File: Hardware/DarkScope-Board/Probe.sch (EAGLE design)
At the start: 3 parts, among them IC1 TL084D, X1 1-227161-0, X4 2540-5

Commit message: Sim Model DP
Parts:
- IC1: SPICEPREFIX (none) -> X
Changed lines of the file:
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@@
 <part name="P+6" library="supply1" library_urn="urn:adsk.eagle:library:371" deviceset="+5V" device=""/>
 <part name="P-2" library="supply1" library_urn="urn:adsk.eagle:library:371" deviceset="-5V" device=""/>
-<part name="IC1" library="linear" library_urn="urn:adsk.eagle:library:262" deviceset="TL084" device="D" package3d_urn="urn:adsk.eagle:package:16406/2"/>
+<part name="IC1" library="linear" library_urn="urn:adsk.eagle:library:262" deviceset="TL084" device="D" package3d_urn="urn:adsk.eagle:package:16406/2">
+<attribute name="SPICEPREFIX" value="X"/>
+</part>
 <part name="X1" library="con-coax" library_urn="urn:adsk.eagle:library:133" deviceset="?227161*" device="1-" package3d_urn="urn:adsk.eagle:package:6212/1" technology="-0"/>
 </parts>

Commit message: DP Probe SCH
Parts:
- added C1, C2, C6, C7: 0.1u, rcl:C-EUC1206
- added C3: (no value), capacitor-wima:C2,5-3
- added C4, C5: (no value), rcl:C-TRIMM808
- added R1, R12, R4, R9: 10K, rcl:R-US_R0805
- added R10, R13, R2: 3.3K, rcl:R-US_R0805
- added R11, R14, R3: 1.5K, rcl:R-US_R0805
- added R5, R6, R7, R8: (no value), rcl:R-EU_0204/7
- added S1, S2, S3: EG2301, SamacSys_Parts:EG2301
- added TP1, TP2, TP3, TP4: TPB1,27, testpad:TPB1,27
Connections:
- new net N$1: C6.2, S1.1, TP1.TP, X1.1
- new net N$10: S3.3
- new net N$11: R10.1, R9.2, S2.7
- new net N$12: R11.1, S2.6
- new net N$13: R12.2, R13.1, S3.7
- new net N$14: R14.1, S3.6
- new net N$15: IC1B.-IN, IC1B.OUT
- new net N$2: C6.1, S1.3
- new net N$3: R3.1, S1.6
- new net N$4: R1.2, R2.1, S1.7
- new net N$5: C1.2, C2.2, C7.2, R4.1, R5.1, R7.2, S1.2
- new net N$6: C3.1, C4.E, C7.1, R7.1, R8.1, S2.4
- new net N$7: C1.1, R4.2, S2.1
- new net N$8: C2.1, C5.E, R5.2, R6.2, S2.3
- new net N$9: IC1B.+IN, S2.2
- new net VSENSEL1: R11.2, R14.2, TP3.TP, TP4.TP
- net +5V: now also R1.1, R12.1, R9.1, S1.5, S2.5, S3.5
- net CPLSEL: now also R3.2, TP2.TP
- net GND: now also C3.2, C4.A, C5.A, R10.2, R13.2, R2.2, R6.1, R8.2, S1.4, S1.8, S1.MH1, S1.MH2, S1.MH3, S1.MH4, S2.8, S2.MH1, S2.MH2, S2.MH3, S2.MH4, S3.8, S3.MH1, S3.MH2, S3.MH3, S3.MH4, X1.2
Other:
- note added: "AC"
- note added: "DC"
- note added: "GND"
- moved on the sheet: IC1A, IC1B, IC1C, IC1D

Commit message: Drafted Sch for Probe Board
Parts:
- added C8: 120pF, capacitor-wima:C2,5-3
- added C9: 0.1u, capacitor-wima:C2,5-3
- added R15: 300E, rcl:R-EU_0204/7
- added R16: 120e, rcl:R-US_R0805
- added R17: 180E, rcl:R-EU_0204/7
- added R18: 120E, rcl:R-EU_0204/7
- added R19: 1K, rcl:R-US_R0805
- added R20: 3K, rcl:R-US_R0805
- added R21: 150E, rcl:R-US_R0805
- added R22: 120E, rcl:R-US_R0805
- added R23: 100k, rcl:R-US_R0805
- added R24: 100K, rcl:R-US_R0805
- added R25: 1k, rcl:R-US_R0805
- added TP5, TP6, TP7, TP8: TPB1,27, testpad:TPB1,27
- C1: value 0.1u -> 220pF
- C2: value 0.1u -> 3pF
- C3: value (none) -> 120pF
- C4, C5: value (none) -> 30pF
- C7: value 0.1u -> 1pF
- R4: value 10K -> 100K
- R5: value (none) -> 1.8M 1%
- R6: value (none) -> 200K 1%
- R7: value (none) -> 2M 1%
- R8: value (none) -> 20K 1%
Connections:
- removed net VSENSEL3: X4-24.KL
- removed net VSENSEL4: X4-25.KL
- new net N$16: IC1C.+IN, S3.2
- new net N$17: R17.1, R18.2, S3.4
- new net N$19: S3.1
- new net N$20: IC1C.-IN, R19.1, R20.1, R21.1
- new net N$22: IC1D.+IN, R16.2, R23.1
- new net N$23: IC1C.OUT, R16.1, R19.2, R22.1
- new net N$24: C9.1, IC1D.-IN, R24.1, TP7.TP
- new net N&123: IC1D.OUT, R23.2, R25.1, TP6.TP
- new net VSENSEL2: R14.2, TP4.TP, X4-25.KL
- net -5V: now also R20.2
- net ADCIN: now also C8.1, R22.2
- net GND: now also C8.2, C9.2, R18.1, R21.2
- net N$10: now also R15.1, R17.2
- net N$15: now also R15.2, TP5.TP
- net TL_PWM: now also R24.2
- net TRIG: now also R25.2
- net VSENSEL1: now also X4-24.KL; no longer R14.2, TP4.TP
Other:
- moved on the sheet: IC1C, IC1D, R12, R13, R14, S3, TP4

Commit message: DP wtf
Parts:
- added C10, C11: 0.1uF, rcl:C-EUC1206
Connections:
- net +5V: now also C10.2, IC1P.V+
- net -5V: now also C11.2, IC1P.V-
- net GND: now also C10.1, C11.1
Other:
- note added: "0.1V"
- note added: "10mV"
- note added: "1V"
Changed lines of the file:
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@@
 <part name="TP7" library="testpad" library_urn="urn:adsk.eagle:library:385" deviceset="TP" device="B1,27" package3d_urn="urn:adsk.eagle:package:27944/2"/>
 <part name="TP8" library="testpad" library_urn="urn:adsk.eagle:library:385" deviceset="TP" device="B1,27" package3d_urn="urn:adsk.eagle:package:27944/2"/>
+<part name="C10" library="rcl" library_urn="urn:adsk.eagle:library:334" deviceset="C-EU" device="C1206" package3d_urn="urn:adsk.eagle:package:23618/2" value="0.1uF"/>
+<part name="C11" library="rcl" library_urn="urn:adsk.eagle:library:334" deviceset="C-EU" device="C1206" package3d_urn="urn:adsk.eagle:package:23618/2" value="0.1uF"/>
+<part name="P+1" library="supply1" library_urn="urn:adsk.eagle:library:371" deviceset="+5V" device=""/>
+<part name="P-3" library="supply1" library_urn="urn:adsk.eagle:library:371" deviceset="-5V" device=""/>
+<part name="P-4" library="supply1" library_urn="urn:adsk.eagle:library:371" deviceset="-5V" device=""/>
+<part name="GND12" library="supply1" library_urn="urn:adsk.eagle:library:371" deviceset="GND" device=""/>
 </parts>
 <sheets>
@@
 <instance part="P-2" gate="1" x="97.79" y="140.97" smashed="yes" rot="R180">
 <attribute name="VALUE" x="100.33" y="143.51" size="1.778" layer="96" rot="R270"/>
+</instance>
+<instance part="P-3" gate="1" x="209.804" y="18.034" smashed="yes" rot="R180">
+<attribute name="VALUE" x="212.344" y="20.574" size="1.778" layer="96" rot="R270"/>
 </instance>
 </instances>
@@
 <text x="55.88" y="78.74" size="1.778" layer="95">AC</text>
 <text x="55.88" y="76.2" size="1.778" layer="95">GND</text>
+<text x="176.53" y="85.344" size="1.778" layer="95">10mV</text>
+<text x="177.038" y="80.01" size="1.778" layer="95">0.1V</text>
+<text x="177.546" y="77.47" size="1.778" layer="95">1V</text>
 </plain>
 <instances>
@@
 </instance>
 <instance part="C7" gate="G$1" x="121.666" y="41.148" smashed="yes" rot="R270">
-<attribute name="NAME" x="122.047" y="39.624" size="1.778" layer="95" rot="R270"/>
-<attribute name="VALUE" x="116.967" y="39.624" size="1.778" layer="96" rot="R270"/>
+<attribute name="NAME" x="122.809" y="45.212" size="1.778" layer="95" rot="R270"/>
+<attribute name="VALUE" x="116.967" y="46.736" size="1.778" layer="96" rot="R270"/>
 </instance>
 <instance part="GND4" gate="1" x="145.542" y="5.334" smashed="yes">
@@
 <attribute name="NAME" x="396.494" y="85.344" size="1.778" layer="95"/>
 <attribute name="TP_SIGNAL_NAME" x="399.034" y="82.804" size="1.778" layer="97"/>
+</instance>
+<instance part="C10" gate="G$1" x="198.374" y="35.814" smashed="yes" rot="R270">
+<attribute name="NAME" x="198.755" y="34.29" size="1.778" layer="95" rot="R270"/>
+<attribute name="VALUE" x="193.675" y="34.29" size="1.778" layer="96" rot="R270"/>
+</instance>
+<instance part="C11" gate="G$1" x="198.882" y="12.446" smashed="yes" rot="R270">
+<attribute name="NAME" x="199.263" y="10.922" size="1.778" layer="95" rot="R270"/>
+<attribute name="VALUE" x="194.183" y="10.922" size="1.778" layer="96" rot="R270"/>
+</instance>
+<instance part="P+1" gate="1" x="188.468" y="40.386" smashed="yes">
+<attribute name="VALUE" x="185.928" y="35.306" size="1.778" layer="96" rot="R90"/>
+</instance>
+<instance part="P-4" gate="1" x="181.102" y="17.526" smashed="yes" rot="R180">
+<attribute name="VALUE" x="183.642" y="20.066" size="1.778" layer="96" rot="R270"/>
+</instance>
+<instance part="GND12" gate="1" x="208.534" y="24.13" smashed="yes" rot="R90">
+<attribute name="VALUE" x="211.074" y="21.59" size="1.778" layer="96" rot="R90"/>
 </instance>
 </instances>
@@
 <wire x1="398.526" y1="-9.398" x2="398.526" y2="-13.716" width="0.1524" layer="91"/>
 </segment>
+<segment>
+<pinref part="C10" gate="G$1" pin="1"/>
+<wire x1="200.914" y1="35.814" x2="204.216" y2="35.814" width="0.1524" layer="91"/>
+<wire x1="204.216" y1="35.814" x2="204.216" y2="24.13" width="0.1524" layer="91"/>
+<pinref part="C11" gate="G$1" pin="1"/>
+<wire x1="204.216" y1="24.13" x2="204.216" y2="12.446" width="0.1524" layer="91"/>
+<wire x1="204.216" y1="12.446" x2="201.422" y2="12.446" width="0.1524" layer="91"/>
+<pinref part="GND12" gate="1" pin="GND"/>
+<wire x1="205.994" y1="24.13" x2="204.216" y2="24.13" width="0.1524" layer="91"/>
+<junction x="204.216" y="24.13"/>
+</segment>
 </net>
 <net name="N$4" class="0">
@@
 <wire x1="304.292" y1="55.626" x2="307.086" y2="55.626" width="0.1524" layer="91"/>
 <junction x="307.086" y="55.626"/>
+</segment>
+<segment>
+<pinref part="IC1" gate="P" pin="V+"/>
+<pinref part="C10" gate="G$1" pin="2"/>
+<wire x1="188.468" y1="31.496" x2="188.468" y2="35.814" width="0.1524" layer="91"/>
+<wire x1="188.468" y1="35.814" x2="193.294" y2="35.814" width="0.1524" layer="91"/>
+<pinref part="P+1" gate="1" pin="+5V"/>
+<wire x1="188.468" y1="37.846" x2="188.468" y2="35.814" width="0.1524" layer="91"/>
+<junction x="188.468" y="35.814"/>
 </segment>
 </net>
@@
 <wire x1="401.828" y1="56.896" x2="401.828" y2="64.77" width="0.1524" layer="91"/>
 </segment>
-</net>
+<segment>
+<pinref part="IC1" gate="P" pin="V-"/>
+<pinref part="C11" gate="G$1" pin="2"/>
+<wire x1="188.468" y1="16.256" x2="188.468" y2="12.446" width="0.1524" layer="91"/>
+<wire x1="188.468" y1="12.446" x2="193.802" y2="12.446" width="0.1524" layer="91"/>
+<pinref part="P-4" gate="1" pin="-5V"/>
+<wire x1="181.102" y1="14.986" x2="181.102" y2="12.446" width="0.1524" layer="91"/>
+<wire x1="181.102" y1="12.446" x2="188.468" y2="12.446" width="0.1524" layer="91"/>
+<junction x="188.468" y="12.446"/>
+</segment>
+</net>

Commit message: Unrouted Probe Board
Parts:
- S1: value EG2301 -> DC-AC-GND
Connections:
- new net N$21: IC1A.-IN, IC1A.OUT
- net GND: now also IC1A.+IN
- net N$23: now also TP8.TP
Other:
- moved on the sheet: IC1A, TP8
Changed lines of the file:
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@@
 <setting verticaltext="up"/>
 </settings>
-<grid distance="0.01" unitdist="inch" unit="inch" style="lines" multiple="1" display="no" altdistance="0.01" altunitdist="inch" altunit="inch"/>
+<grid distance="0.1" unitdist="inch" unit="inch" style="lines" multiple="1" display="no" altdistance="0.01" altunitdist="inch" altunit="inch"/>
 <layers>
 <layer number="1" name="Top" color="4" fill="1" visible="no" active="no"/>
@@
 </part>
 <part name="X1" library="con-coax" library_urn="urn:adsk.eagle:library:133" deviceset="?227161*" device="1-" package3d_urn="urn:adsk.eagle:package:6212/1" technology="-0"/>
-<part name="S1" library="SamacSys_Parts" deviceset="EG2301" device=""/>
+<part name="S1" library="SamacSys_Parts" deviceset="EG2301" device="" value="DC-AC-GND"/>
 <part name="TP1" library="testpad" library_urn="urn:adsk.eagle:library:385" deviceset="TP" device="B1,27" package3d_urn="urn:adsk.eagle:package:27944/2"/>
 <part name="C6" library="rcl" library_urn="urn:adsk.eagle:library:334" deviceset="C-EU" device="C1206" package3d_urn="urn:adsk.eagle:package:23618/2" value="0.1u"/>
@@
 <part name="P-4" library="supply1" library_urn="urn:adsk.eagle:library:371" deviceset="-5V" device=""/>
 <part name="GND12" library="supply1" library_urn="urn:adsk.eagle:library:371" deviceset="GND" device=""/>
+<part name="GND13" library="supply1" library_urn="urn:adsk.eagle:library:371" deviceset="GND" device=""/>
 </parts>
 <sheets>
@@
 </plain>
 <instances>
-<instance part="IC1" gate="A" x="99.06" y="187.96" smashed="yes">
-<attribute name="NAME" x="101.6" y="191.135" size="1.778" layer="95"/>
-<attribute name="VALUE" x="101.6" y="182.88" size="1.778" layer="96"/>
+<instance part="IC1" gate="A" x="259.08" y="27.94" smashed="yes">
+<attribute name="NAME" x="261.62" y="31.115" size="1.778" layer="95"/>
+<attribute name="VALUE" x="261.62" y="22.86" size="1.778" layer="96"/>
 </instance>
 <instance part="IC1" gate="B" x="251.968" y="81.026" smashed="yes">
@@
 <attribute name="TP_SIGNAL_NAME" x="376.428" y="-0.508" size="1.778" layer="97" rot="R90"/>
 </instance>
-<instance part="TP8" gate="G$1" x="397.764" y="84.074" smashed="yes">
-<attribute name="NAME" x="396.494" y="85.344" size="1.778" layer="95"/>
-<attribute name="TP_SIGNAL_NAME" x="399.034" y="82.804" size="1.778" layer="97"/>
+<instance part="TP8" gate="G$1" x="397.764" y="86.614" smashed="yes">
+<attribute name="NAME" x="396.494" y="87.884" size="1.778" layer="95"/>
+<attribute name="TP_SIGNAL_NAME" x="399.034" y="85.344" size="1.778" layer="97"/>
 </instance>
 <instance part="C10" gate="G$1" x="198.374" y="35.814" smashed="yes" rot="R270">
@@
 <instance part="GND12" gate="1" x="208.534" y="24.13" smashed="yes" rot="R90">
 <attribute name="VALUE" x="211.074" y="21.59" size="1.778" layer="96" rot="R90"/>
+</instance>
+<instance part="GND13" gate="1" x="244.094" y="30.48" smashed="yes" rot="R270">
+<attribute name="VALUE" x="241.554" y="33.02" size="1.778" layer="96" rot="R270"/>
 </instance>
 </instances>
@@
 <junction x="204.216" y="24.13"/>
 </segment>
+<segment>
+<pinref part="IC1" gate="A" pin="+IN"/>
+<pinref part="GND13" gate="1" pin="GND"/>
+<wire x1="251.46" y1="30.48" x2="246.634" y2="30.48" width="0.1524" layer="91"/>
+</segment>
 </net>
 <net name="N$4" class="0">
@@
 <wire x1="397.764" y1="81.28" x2="391.16" y2="81.28" width="0.1524" layer="91"/>
 <pinref part="R22" gate="G$1" pin="1"/>
-<wire x1="403.098" y1="81.28" x2="397.764" y2="81.28" width="0.1524" layer="91"/>
+<wire x1="403.098" y1="81.28" x2="398.78" y2="81.28" width="0.1524" layer="91"/>
 <junction x="397.764" y="81.28"/>
 <wire x1="409.956" y1="73.152" x2="397.764" y2="73.152" width="0.1524" layer="91"/>
 <junction x="397.764" y="73.152"/>
+<pinref part="TP8" gate="G$1" pin="TP"/>
+<wire x1="397.764" y1="84.074" x2="397.764" y2="81.28" width="0.1524" layer="91"/>
+<wire x1="397.764" y1="81.28" x2="398.78" y2="81.28" width="0.1524" layer="91"/>
 </segment>
 </net>
@@
 </segment>
 </net>
+<net name="N$21" class="0">
+<segment>
+<pinref part="IC1" gate="A" pin="-IN"/>
+<wire x1="251.46" y1="25.4" x2="245.872" y2="25.4" width="0.1524" layer="91"/>
+<wire x1="245.872" y1="25.4" x2="245.872" y2="17.526" width="0.1524" layer="91"/>
+<wire x1="245.872" y1="17.526" x2="274.32" y2="17.526" width="0.1524" layer="91"/>
+<wire x1="274.32" y1="17.526" x2="274.32" y2="27.94" width="0.1524" layer="91"/>
+<pinref part="IC1" gate="A" pin="OUT"/>
+<wire x1="274.32" y1="27.94" x2="266.7" y2="27.94" width="0.1524" layer="91"/>
+</segment>
+</net>

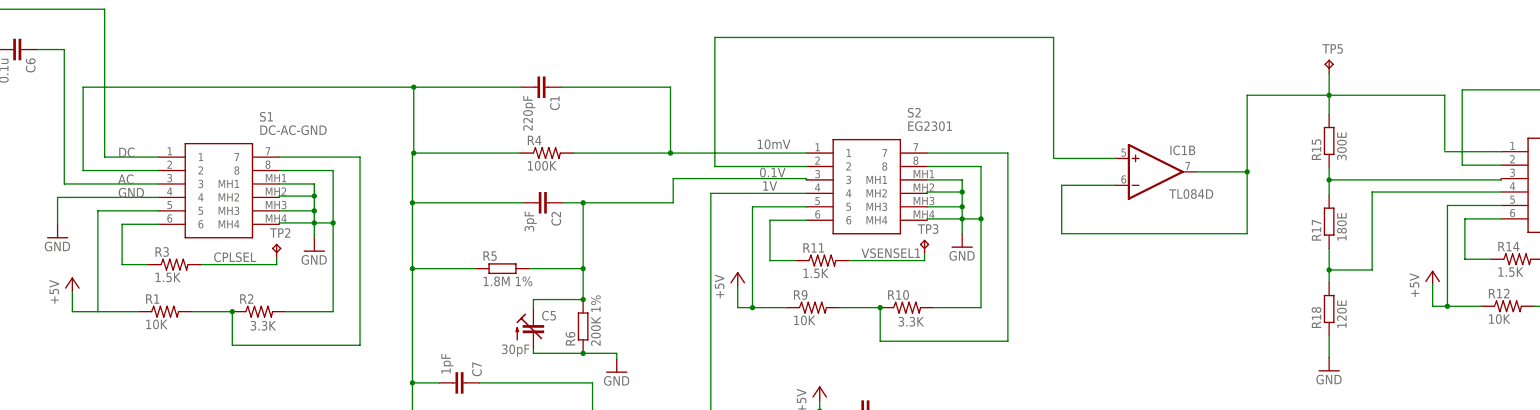
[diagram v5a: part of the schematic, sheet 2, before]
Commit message: Cleared and Fixed Probe Board's ERC Errors
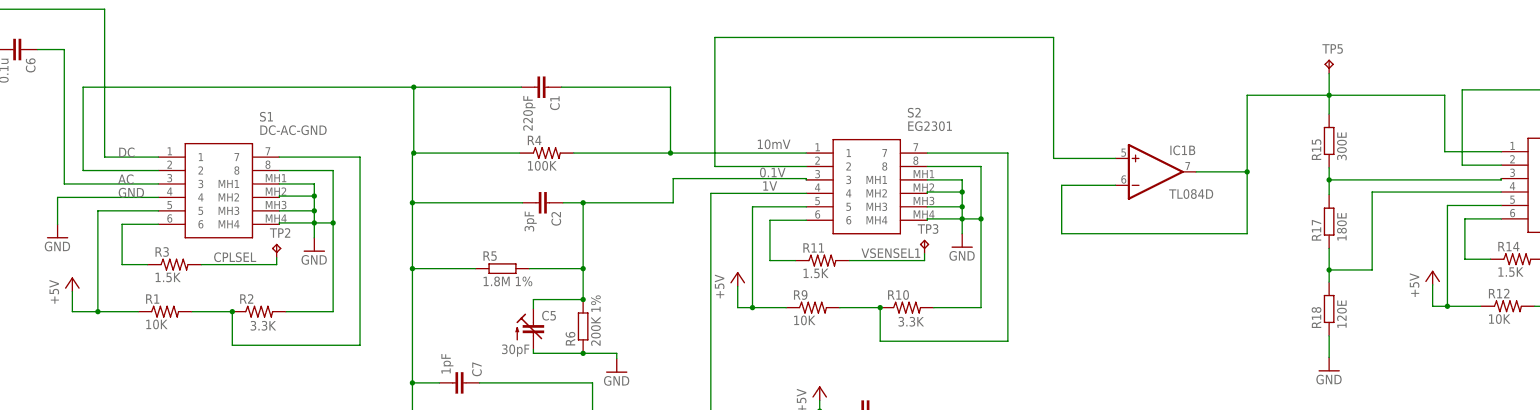
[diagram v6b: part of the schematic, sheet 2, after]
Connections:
- removed net N$15: IC1B.-IN, IC1B.OUT, R15.2, TP5.TP
- removed net N$19: S3.1
- new net N$18: IC1B.-IN, IC1B.OUT, R15.2, S3.1, TP5.TP
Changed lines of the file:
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@@
 <setting verticaltext="up"/>
 </settings>
-<grid distance="0.1" unitdist="inch" unit="inch" style="lines" multiple="1" display="no" altdistance="0.01" altunitdist="inch" altunit="inch"/>
+<grid distance="0.01" unitdist="inch" unit="inch" style="lines" multiple="1" display="no" altdistance="0.01" altunitdist="inch" altunit="inch"/>
 <layers>
 <layer number="1" name="Top" color="4" fill="1" visible="no" active="no"/>
@@
 <wire x1="47.244" y1="58.42" x2="47.244" y2="54.61" width="0.1524" layer="91"/>
 <wire x1="47.244" y1="54.61" x2="52.07" y2="54.61" width="0.1524" layer="91"/>
+<junction x="52.07" y="54.61"/>
 </segment>
 <segment>
@@
 </segment>
 </net>
-<net name="N$15" class="0">
-<segment>
-<pinref part="IC1" gate="B" pin="-IN"/>
-<wire x1="244.348" y1="78.486" x2="234.188" y2="78.486" width="0.1524" layer="91"/>
-<wire x1="234.188" y1="78.486" x2="234.188" y2="69.342" width="0.1524" layer="91"/>
-<wire x1="234.188" y1="69.342" x2="269.24" y2="69.342" width="0.1524" layer="91"/>
-<wire x1="269.24" y1="69.342" x2="269.24" y2="81.026" width="0.1524" layer="91"/>
-<pinref part="IC1" gate="B" pin="OUT"/>
-<wire x1="259.588" y1="81.026" x2="269.24" y2="81.026" width="0.1524" layer="91"/>
-<pinref part="R15" gate="G$1" pin="2"/>
-<pinref part="TP5" gate="G$1" pin="TP"/>
-<wire x1="284.734" y1="99.568" x2="284.734" y2="95.504" width="0.1524" layer="91"/>
-<wire x1="284.734" y1="95.504" x2="284.734" y2="91.948" width="0.1524" layer="91"/>
-<wire x1="269.24" y1="81.026" x2="269.24" y2="95.504" width="0.1524" layer="91"/>
-<wire x1="269.24" y1="95.504" x2="284.734" y2="95.504" width="0.1524" layer="91"/>
-<junction x="269.24" y="81.026"/>
-<junction x="284.734" y="95.504"/>
-</segment>
-</net>
 <net name="N$17" class="0">
 <segment>
@@
 <net name="N$18" class="0">
 <segment>
-<wire x1="285.242" y1="95.504" x2="306.578" y2="95.504" width="0.1524" layer="91"/>
-<wire x1="306.578" y1="95.504" x2="306.578" y2="85.09" width="0.1524" layer="91"/>
-</segment>
-</net>
-<net name="N$19" class="0">
-<segment>
+<wire x1="269.24" y1="95.504" x2="284.734" y2="95.504" width="0.1524" layer="91"/>
+<wire x1="284.734" y1="95.504" x2="306.578" y2="95.504" width="0.1524" layer="91"/>
+<wire x1="306.578" y1="95.504" x2="306.578" y2="84.836" width="0.1524" layer="91"/>
 <pinref part="S3" gate="G$1" pin="1"/>
 <wire x1="306.578" y1="84.836" x2="317.246" y2="84.836" width="0.1524" layer="91"/>
+<pinref part="IC1" gate="B" pin="-IN"/>
+<wire x1="244.348" y1="78.486" x2="234.188" y2="78.486" width="0.1524" layer="91"/>
+<wire x1="234.188" y1="78.486" x2="234.188" y2="69.342" width="0.1524" layer="91"/>
+<wire x1="234.188" y1="69.342" x2="269.24" y2="69.342" width="0.1524" layer="91"/>
+<wire x1="269.24" y1="69.342" x2="269.24" y2="81.026" width="0.1524" layer="91"/>
+<pinref part="IC1" gate="B" pin="OUT"/>
+<wire x1="259.588" y1="81.026" x2="269.24" y2="81.026" width="0.1524" layer="91"/>
+<wire x1="269.24" y1="81.026" x2="269.24" y2="95.504" width="0.1524" layer="91"/>
+<junction x="269.24" y="81.026"/>
+<pinref part="R15" gate="G$1" pin="2"/>
+<pinref part="TP5" gate="G$1" pin="TP"/>
+<wire x1="284.734" y1="99.568" x2="284.734" y2="95.504" width="0.1524" layer="91"/>
+<junction x="284.734" y="95.504"/>
+<wire x1="284.734" y1="95.504" x2="284.734" y2="91.948" width="0.1524" layer="91"/>
 </segment>
 </net>
@@
 </sheet>
 </sheets>
+<errors>
+</errors>
 </schematic>
 </drawing>
